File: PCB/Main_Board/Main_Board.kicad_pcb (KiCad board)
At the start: 2 copper layers, 49 parts, among them J1 USB_B_Micro, J3 SJ1-3523N, J4 SJ1-3523N, Q1 MBT3904DW1, SW1 SW_SPDT, SW2 EN, SW3 BOOT, U1 TLV75533PDBV, U3 ESP32-WROOM-32, U4 FT231XS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

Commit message: PCB Layout work
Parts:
- added J2: Screw_Terminal_01x02, TerminalBlock:TerminalBlock_bornier-2_P5.08mm, F.Cu at (25.8, 87.2)
- added J5: Screw_Terminal_01x04, TerminalBlock_Phoenix:TerminalBlock_Phoenix_MPT-0,5-4-2.54_1x04_P2.54mm_Horizontal, F.Cu at (85.5, 87.0)
- added J6: Screw_Terminal_01x06, TerminalBlock_Phoenix:TerminalBlock_Phoenix_MPT-0,5-6-2.54_1x06_P2.54mm_Horizontal, F.Cu at (107.2, 52.8)
- C13, C17: value 0.01uF -> 10nF
- R1: value CUR_LIMIT -> CUR_LIMIT_5.6R
- R7, R8: value CUR_LIMIT -> CUR_LIMIT_100R
- moved J1 147.3 mm to (170.1, 67.2), turned to 90 degrees
- moved SW3 120.0 mm to (162.9, 57.0)
- moved C7 115.2 mm to (171.7, 59.3), turned to 270 degrees
- moved SW2 115.2 mm to (162.8, 47.9)
- moved C8 111.9 mm to (158.8, 64.8), turned to 270 degrees
- moved C11 109.6 mm to (160.3, 61.4), turned to 270 degrees
- moved R6 105.7 mm to (156.3, 63.9)
- moved D5 105.0 mm to (152.8, 54.6)
- moved C6 104.4 mm to (171.6, 50.2), turned to 270 degrees
- moved C12 104.2 mm to (158.8, 61.3), turned to 270 degrees
- moved R5 102.7 mm to (156.3, 65.4)
- moved R7 101.2 mm to (149.4, 54.6), turned to 180 degrees
- moved R8 100.2 mm to (149.4, 53.1), turned to 180 degrees
- moved C9 100.1 mm to (156.4, 66.9), turned to 180 degrees
- moved U4 97.9 mm to (151.1, 61.5)
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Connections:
- VR1 pad 1: Net-(C13-Pad1) -> Net-(VR1-Pad1)
- VR1 pad 3: Net-(VR1-Pad3) -> Net-(C13-Pad1)
- VR2 pad 1: Net-(R9-Pad1) -> Net-(VR2-Pad1)
- VR2 pad 3: Net-(VR2-Pad3) -> Net-(R9-Pad1)
- VR3 pad 1: Net-(C17-Pad1) -> Net-(VR3-Pad1)
- VR3 pad 3: Net-(VR3-Pad3) -> Net-(C17-Pad1)
- VR4 pad 1: Net-(R10-Pad1) -> Net-(VR4-Pad1)
- VR4 pad 3: Net-(VR4-Pad3) -> Net-(R10-Pad1)
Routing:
- net Earth: track 0.00 -> 84.1 mm, vias 0 -> 22
- net /AUDIO_R: track 0.00 -> 51.8 mm
- net /AUDIO_L: track 0.00 -> 36.0 mm
- net /+USB_5V: track 0.00 -> 29.8 mm
- net /LED_OUT: track 0.00 -> 21.6 mm
- net /MSGEQ7_RESET: track 0.00 -> 19.2 mm
- net /ESP32_Circuit/EN: track 0.00 -> 18.3 mm
- net /+3.3V: track 0.00 -> 17.4 mm
- net /ESP32_Circuit/~DTR: track 0.00 -> 17.1 mm, vias 0 -> 2
- net /ESP32_Circuit/IO0: track 0.00 -> 16.3 mm
- net /ESP32_Circuit/~RTS: track 0.00 -> 15.7 mm, vias 0 -> 2
- net /MSGEQ7_STROBE: track 0.00 -> 13.5 mm
- net Net-(R8-Pad2): track 0.00 -> 13.5 mm
- net /D+: track 0.00 -> 13.3 mm, vias 0 -> 2
- net /D-: track 0.00 -> 13.1 mm, vias 0 -> 2
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- added copper zone on F.Cu, net /+3.3V
- added copper zone on B.Cu, net Earth
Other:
- board text added: "3.3V"
- board text added: "IR"
- board text added: "L"
- board text added: "R"

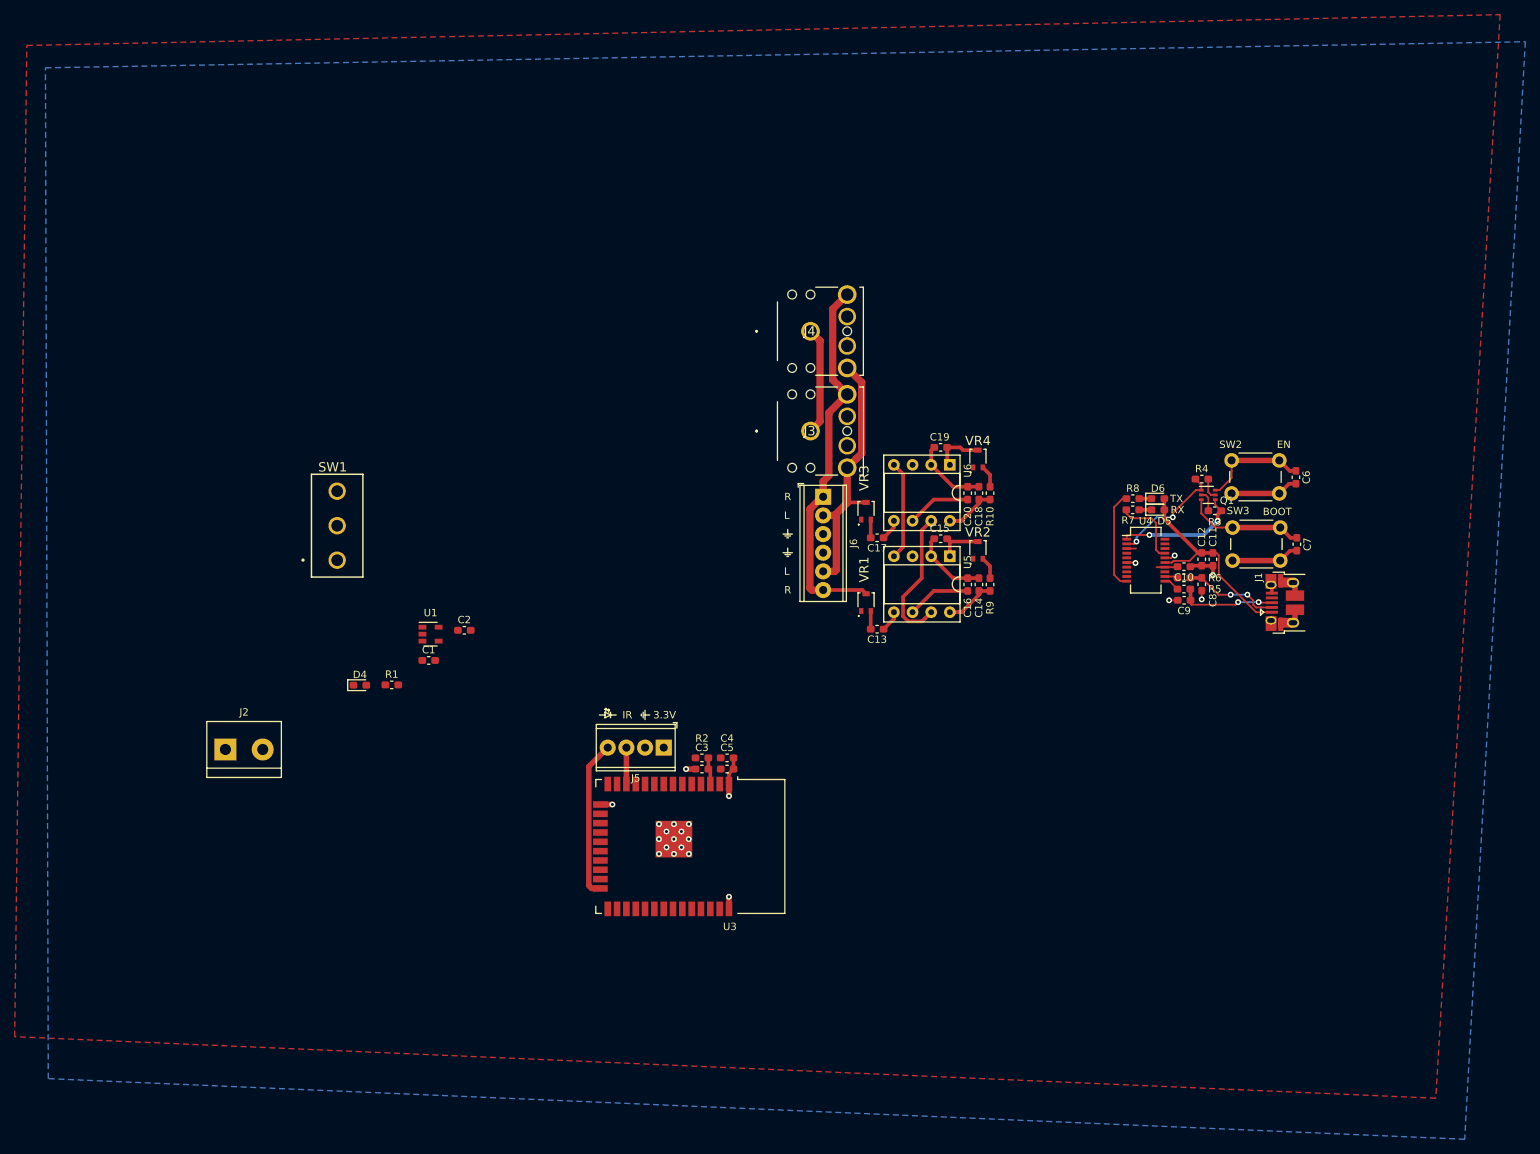
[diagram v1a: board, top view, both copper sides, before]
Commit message: Add level shifter and further PCB work
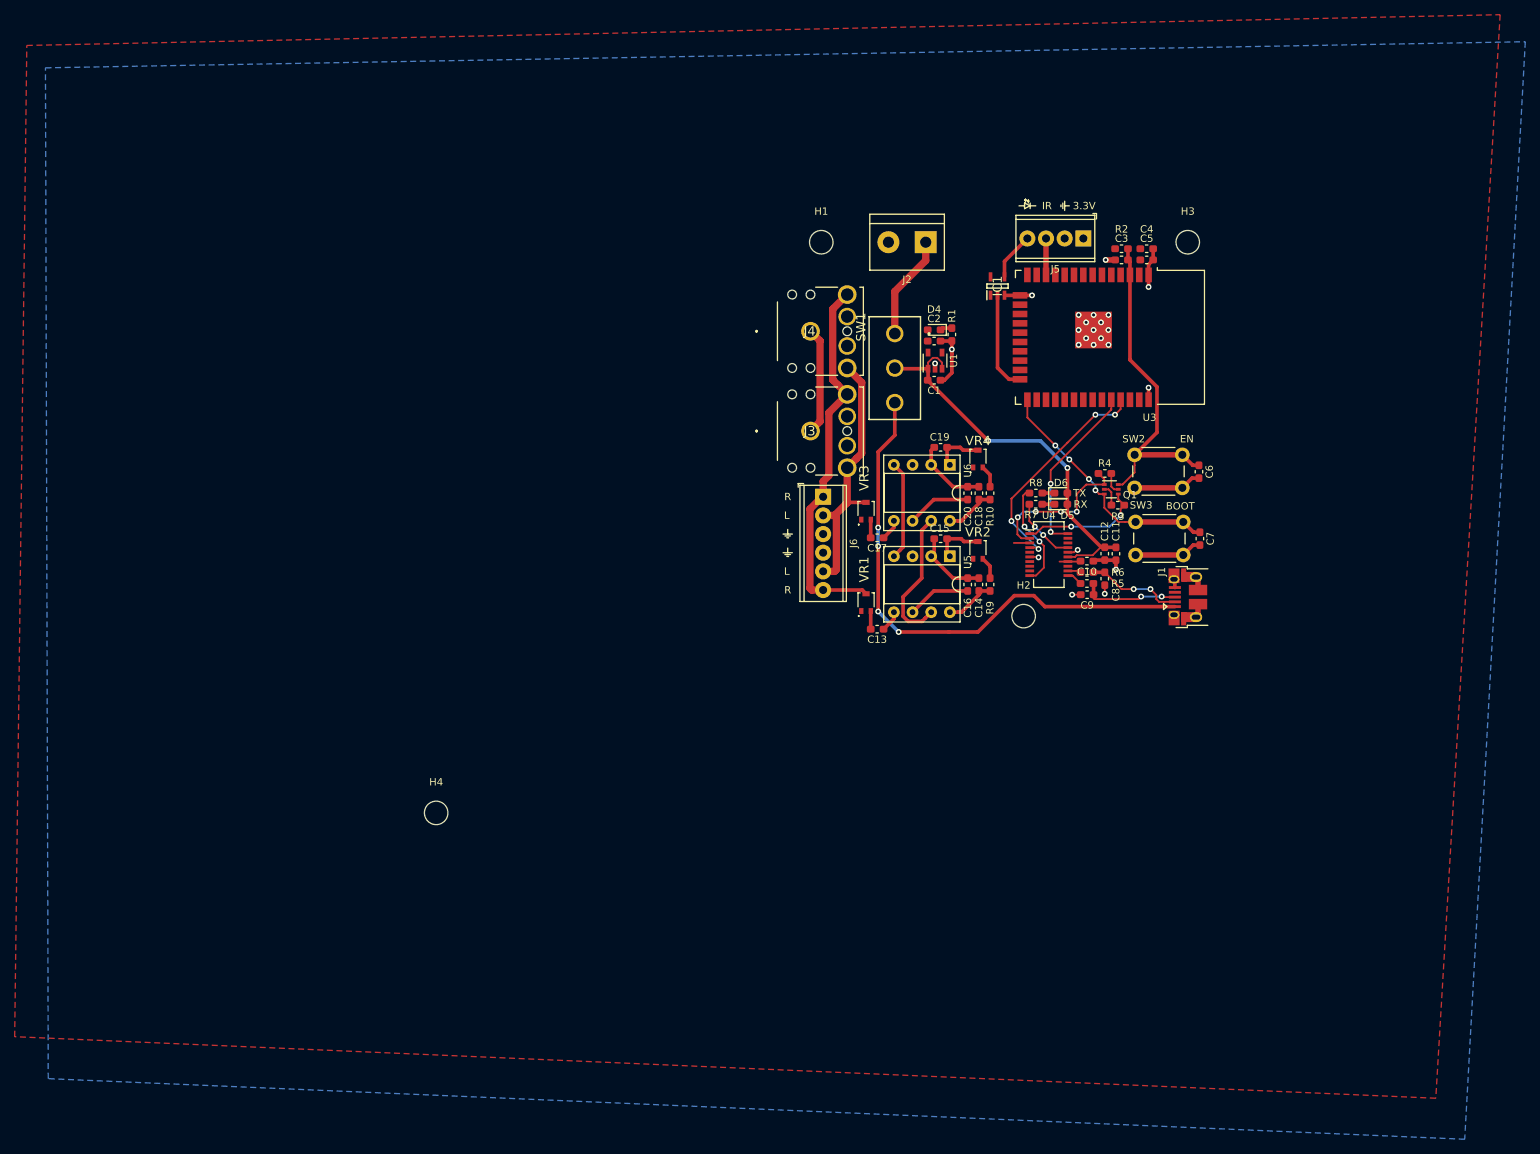
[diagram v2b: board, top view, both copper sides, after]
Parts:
- added H1: MountingHole, MountingHole:MountingHole_3.2mm_M3, F.Cu at (106.9, 18.2)
- added H2: MountingHole, MountingHole:MountingHole_3.2mm_M3, F.Cu at (134.5, 69.1)
- added H3: MountingHole, MountingHole:MountingHole_3.2mm_M3, F.Cu at (156.8, 18.2)
- added H4: MountingHole, MountingHole:MountingHole_3.2mm_M3, F.Cu at (54.5, 95.9)
- added IC1: 74LV1T34GVH, SamacSys:SOT95P275X110-5N, F.Cu at (130.9, 24.1)
- moved J2 117.8 mm to (121.2, 18.2), turned to 180 degrees
- moved D4 92.0 mm to (122.3, 30.1), turned to 180 degrees
- moved R1 90.0 mm to (124.7, 30.7), turned to 270 degrees
- moved J5 89.9 mm to (142.6, 17.7)
- moved C3 89.9 mm to (147.8, 20.6)
- moved C4 89.9 mm to (151.3, 19.1)
- moved C5 89.9 mm to (151.3, 20.6)
- moved R2 89.9 mm to (147.8, 19.1)
- moved U3 89.9 mm to (143.3, 31.1)
- moved SW1 78.9 mm to (116.9, 35.3), turned to 180 degrees
- moved C1 78.7 mm to (122.3, 37.0)
- moved U1 78.2 mm to (122.4, 34.3), turned to 90 degrees
- moved C2 75.1 mm to (122.3, 31.6)
- moved R8 13.2 mm to (136.2, 52.3)
- moved C10 13.2 mm to (143.1, 61.6)
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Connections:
- C1 pad 1: Net-(C1-Pad1) -> /+5V
- C11 pad 1: /+USB_5V -> /+5V
- C12 pad 1: /+USB_5V -> /+5V
- D5 pad 2: /+USB_5V -> /+5V
- D6 pad 2: /+USB_5V -> /+5V
- J5 pad 4: /LED_OUT -> /LED_OUT_5V
- SW1 pad 2: Net-(C1-Pad1) -> /+5V
- U1 pad 1: Net-(C1-Pad1) -> /+5V
- U1 pad 3: Net-(C1-Pad1) -> /+5V
- U3 pad 24: /LED_OUT -> /LED_OUT_3.3V
- U4 pad 15: /+USB_5V -> /+5V
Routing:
- net /+5V: track 0.00 -> 54.6 mm, vias 0 -> 2
- net /+USB_5V: track 29.8 -> 73.6 mm, vias 0 -> 4
- net /ESP32_Circuit/IO1_TXD0: track 0.00 -> 30.9 mm, vias 0 -> 4
- net /ESP32_Circuit/EN: track 18.3 -> 45.6 mm
- net /ESP32_Circuit/IO3_RXD0: track 0.00 -> 23.9 mm, vias 0 -> 2
- net /LED_OUT: track 21.6 -> 0.00 mm
- net /ESP32_Circuit/IO0: track 16.3 -> 34.5 mm, vias 0 -> 4
- net /+POW_5V: track 0.00 -> 14.2 mm
- net /LED_OUT_3.3V: track 0.00 -> 13.6 mm
- net Earth: track 84.1 -> 94.8 mm, vias 22 -> 24
- net /LED_OUT_5V: track 0.00 -> 6.52 mm
- net /ESP32_Circuit/~RTS: track 15.7 -> 21.1 mm, vias 2 -> 4
- net Net-(D4-Pad1): track 0.00 -> 1.64 mm
- net /+3.3V: track 17.4 -> 18.9 mm
- net Net-(R7-Pad2): track 10.1 -> 9.05 mm, vias 0 -> 2
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
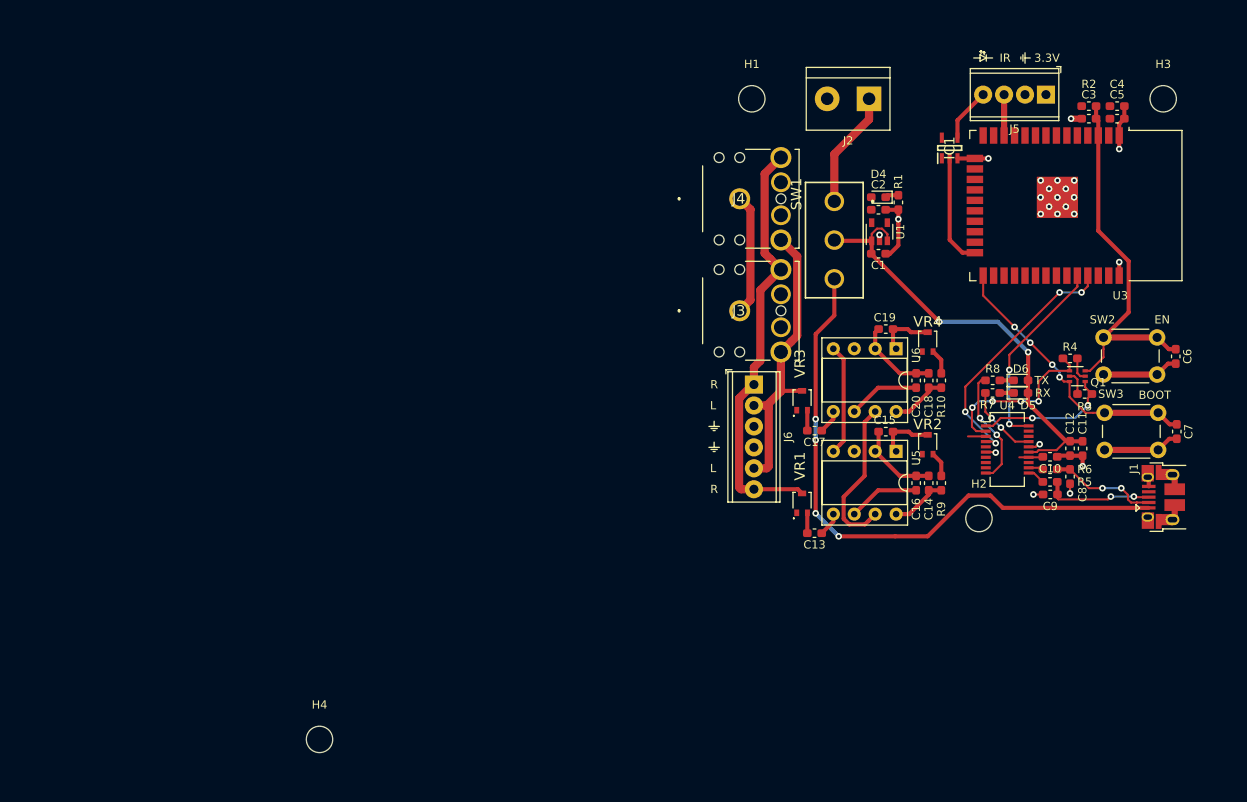
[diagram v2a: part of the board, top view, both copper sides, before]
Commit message: Finish PCB, add missing models, change switch
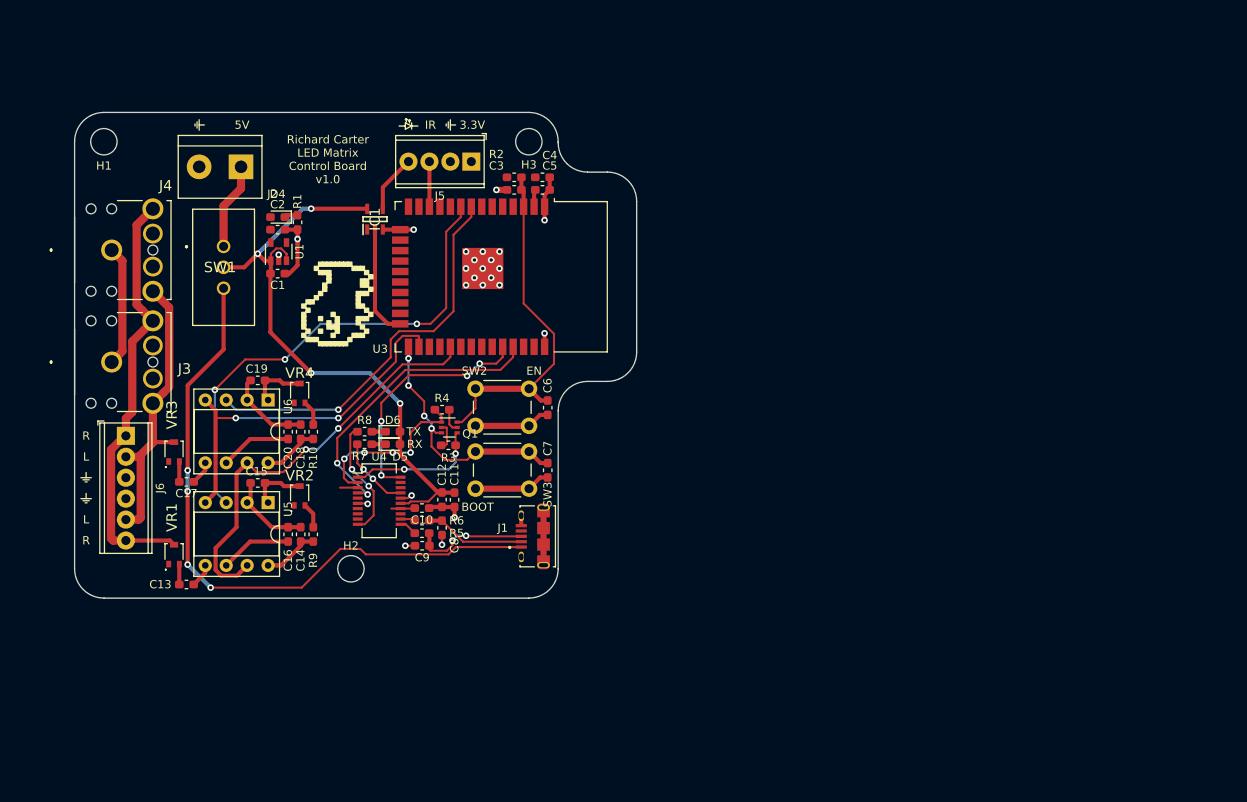
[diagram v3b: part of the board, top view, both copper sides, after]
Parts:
- removed H4: MountingHole, MountingHole:MountingHole_3.2mm_M3
- added U2: Artwork, Artwork:dog_logo, F.Cu at (57.4, 44.1)
- J1: footprint Connector_USB:USB_Micro-B_Amphenol_10103594-0001LF_Horizontal -> SamacSys:AMPHENOL_10118194-0001LF
- SW1: footprint SamacSys:CS12ANW03 -> SamacSys:25136NAH
- moved H1 78.8 mm to (28.3, 23.4)
- moved R3 77.5 mm to (70.1, 60.2)
- moved H3 77.1 mm to (79.9, 23.4)
- moved J2 76.6 mm to (45.0, 26.4)
- moved C7 76.5 mm to (82.2, 63.2)
- moved SW3 76.5 mm to (73.4, 61.0)
- moved D5 76.5 mm to (63.4, 60.1)
- moved D6 76.5 mm to (63.4, 58.5)
- moved Q1 76.5 mm to (70.2, 58.0)
- moved R4 76.5 mm to (69.4, 55.9)
- moved VR2 76.5 mm to (52.1, 66.3)
- moved VR4 76.5 mm to (52.1, 53.9)
- moved C10 76.5 mm to (66.9, 67.8)
- moved C11 76.5 mm to (70.9, 66.8)
- moved C12 76.5 mm to (69.3, 66.8)
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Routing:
- net /MSGEQ7_R_OUT: track 0.00 -> 59.5 mm, vias 0 -> 3
- net /MSGEQ7_L_OUT: track 0.00 -> 47.9 mm, vias 0 -> 1
- net /MSGEQ7_RESET: track 19.2 -> 51.4 mm, vias 0 -> 2
- net /MSGEQ7_STROBE: track 13.5 -> 44.9 mm, vias 0 -> 2
- net /+5V: track 54.6 -> 74.8 mm, vias 2 -> 4
- net /+USB_5V: track 73.6 -> 79.6 mm
- net /ESP32_Circuit/IO3_RXD0: track 23.9 -> 29.6 mm, vias 2 -> 4
- net /ESP32_Circuit/IO1_TXD0: track 30.9 -> 36.3 mm, vias 4 -> 2
- net /ESP32_Circuit/IO0: track 34.5 -> 30.5 mm
- net /+POW_5V: track 14.2 -> 10.5 mm
- net Earth: track 94.8 -> 98.1 mm
- net /+3.3V: track 18.9 -> 21.0 mm
- net /D+: track 13.3 -> 14.4 mm
- net /D-: track 13.1 -> 12.2 mm, vias 2 -> 0
- net /ESP32_Circuit/~DTR: track 16.9 -> 16.3 mm
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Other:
- board outline added: 68.2 x 58.9 mm
- board text added: "5V"
- board text added: "Richard Carter LED Matrix Control Board v1.0"
